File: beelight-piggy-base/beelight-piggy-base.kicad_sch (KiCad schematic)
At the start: 85 parts, among them J1 B_Le, J10 USB C power only, J2 B_Ri, J4 WS2812_ext, J5 Conn_01x07_Pin, J6 BatSide, J7 DevSide, J8 B_Ri, J9 B_Le, Q1 AO3400A, SW1 SW_Push, U2 BMA253, U3 TPS22917LDBV, U4 rysta, U5 VEML3328, U6 TSOP382xx, U7 MP2667, U8 BQ27421-G1

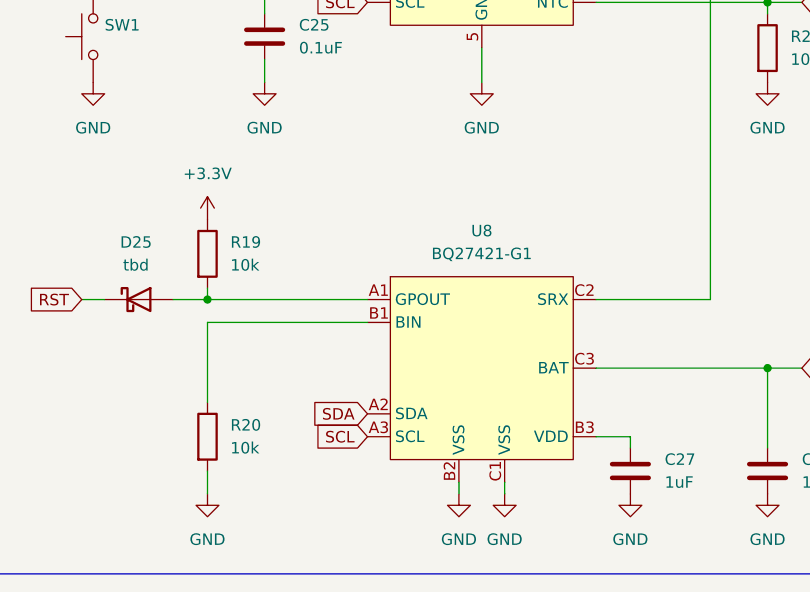
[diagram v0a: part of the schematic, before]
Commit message: rewire gpout pull-up to vdd
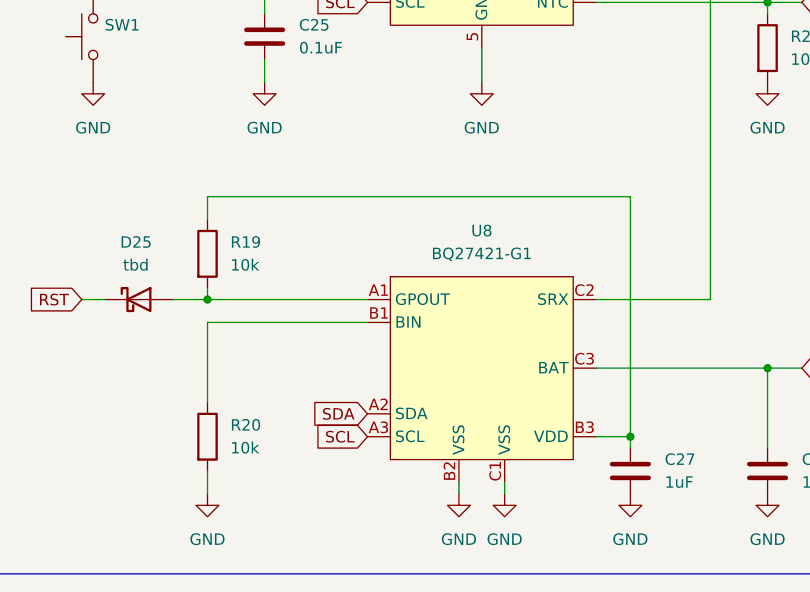
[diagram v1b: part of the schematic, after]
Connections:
- net +3.3V: no longer R19.1
- net at C27.1, U8.B3 (VDD): now also R19.1
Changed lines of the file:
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@@
 	)
 	(junction
+		(at 165.1 241.3)
+		(diameter 0)
+		(color 0 0 0 0)
+	)
+	(junction
 		(at 370.84 120.65)
 		(diameter 0)
@@
 	(wire
 		(pts
+			(xy 165.1 214.63) (xy 165.1 241.3)
+		)
+		(stroke
+			(width 0)
+			(type default)
+		)
+	)
+	(wire
+		(pts
 			(xy 267.97 227.33) (xy 267.97 226.06)
 		)
@@
 	(wire
 		(pts
+			(xy 118.11 217.17) (xy 118.11 214.63)
+		)
+		(stroke
+			(width 0)
+			(type default)
+		)
+	)
+	(wire
+		(pts
 			(xy 261.62 43.18) (xy 261.62 179.07)
 		)
@@
 	(wire
 		(pts
+			(xy 118.11 214.63) (xy 165.1 214.63)
+		)
+		(stroke
+			(width 0)
+			(type default)
+		)
+	)
+	(wire
+		(pts
 			(xy 76.2 120.65) (xy 86.36 120.65)
 		)
@@
 					(unit 1)
 				)
-			)
-		)
-	)
-	(symbol
-		(lib_id "power:+3.3V")
-		(at 118.11 217.17 0)
-		(mirror y)
-		(unit 1)
-		(body_style 1)
-		(exclude_from_sim no)
-		(in_bom yes)
-		(on_board yes)
-		(in_pos_files yes)
-		(dnp no)
-		(property "Reference" "#PWR055"
-			(at 118.11 220.98 0)
-			(hide yes)
-			(show_name no)
-			(do_not_autoplace no)
-			(effects
-				(font
-					(size 1.27 1.27)
-				)
-			)
-		)
-		(property "Value" "+3.3V"
-			(at 118.11 212.09 0)
-			(show_name no)
-			(do_not_autoplace no)
-			(effects
-				(font
-					(size 1.27 1.27)
-				)
-			)
-		)
-		(property "Footprint" ""
-			(at 118.11 217.17 0)
-			(hide yes)
-			(show_name no)
-			(do_not_autoplace no)
-			(effects
-				(font
-					(size 1.27 1.27)
-				)
-			)
-		)
-		(property "Datasheet" ""
-			(at 118.11 217.17 0)
-			(hide yes)
-			(show_name no)
-			(do_not_autoplace no)
-			(effects
-				(font
-					(size 1.27 1.27)
-				)
-			)
-		)
-		(property "Description" "Power symbol creates a global label with name \"+3.3V\""
-			(at 118.11 217.17 0)
-			(hide yes)
-			(show_name no)
-			(do_not_autoplace no)
-			(effects
-				(font
-					(size 1.27 1.27)
-				)
-			)
-		)
-		(pin "1"
-		)
-		(instances
-			(project "beelight-piggy-base"
-				(path "/22ed276f-7cd6-4eef-b98c-6265ea08505b"
-					(reference "#PWR055")
-					(unit 1)
-				)

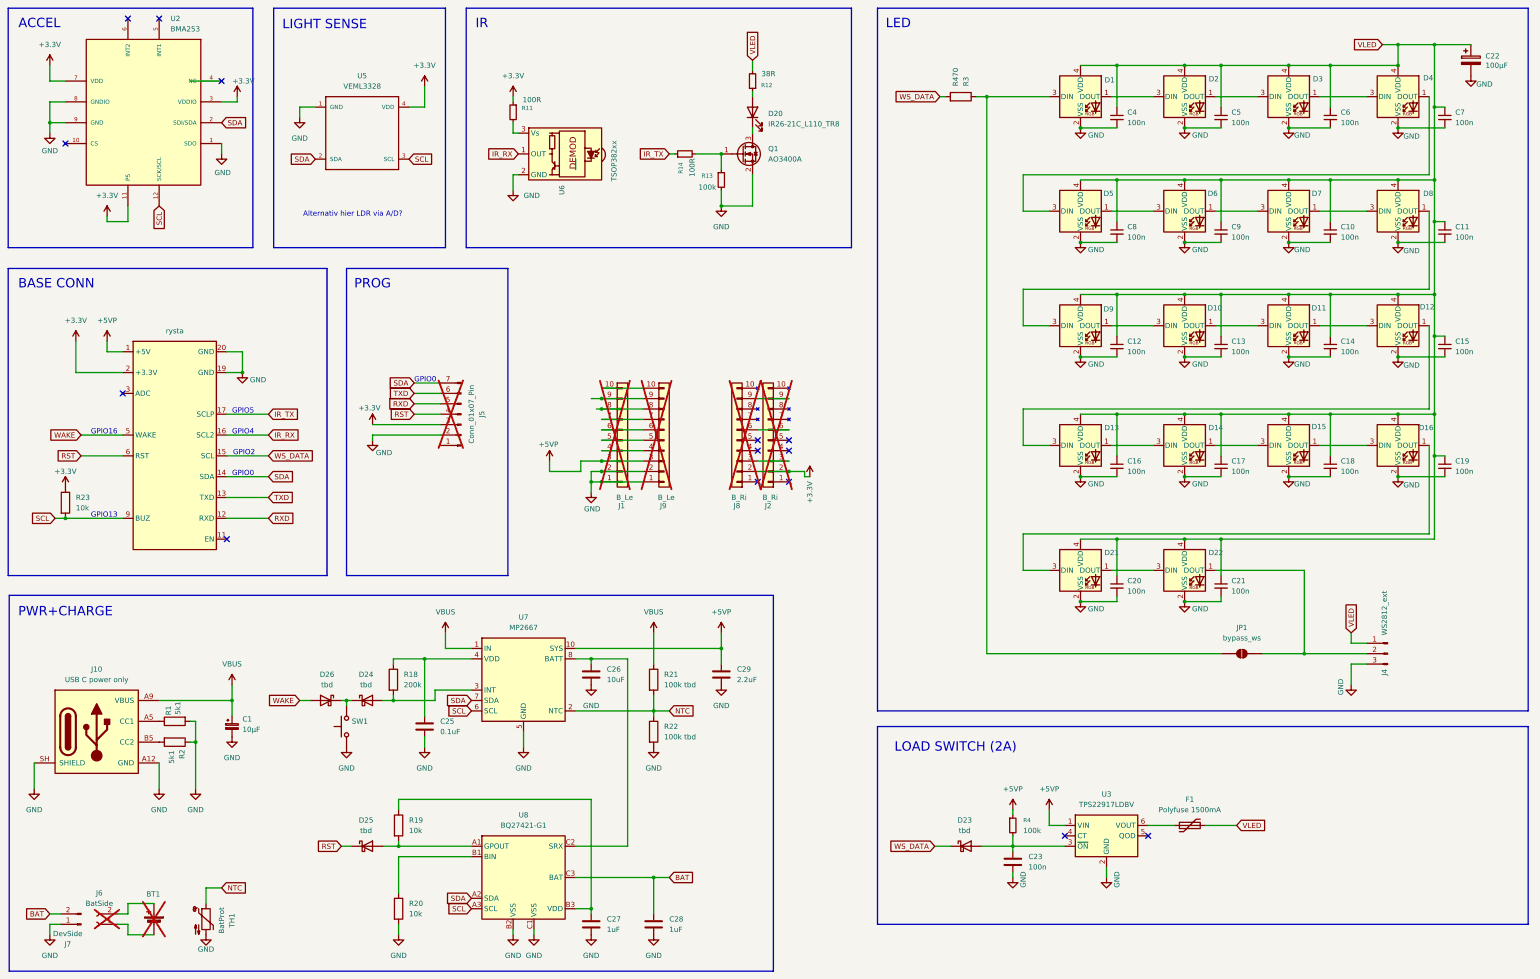
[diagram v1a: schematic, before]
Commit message: ws2816, schottky diodes added, used 0r for jprs
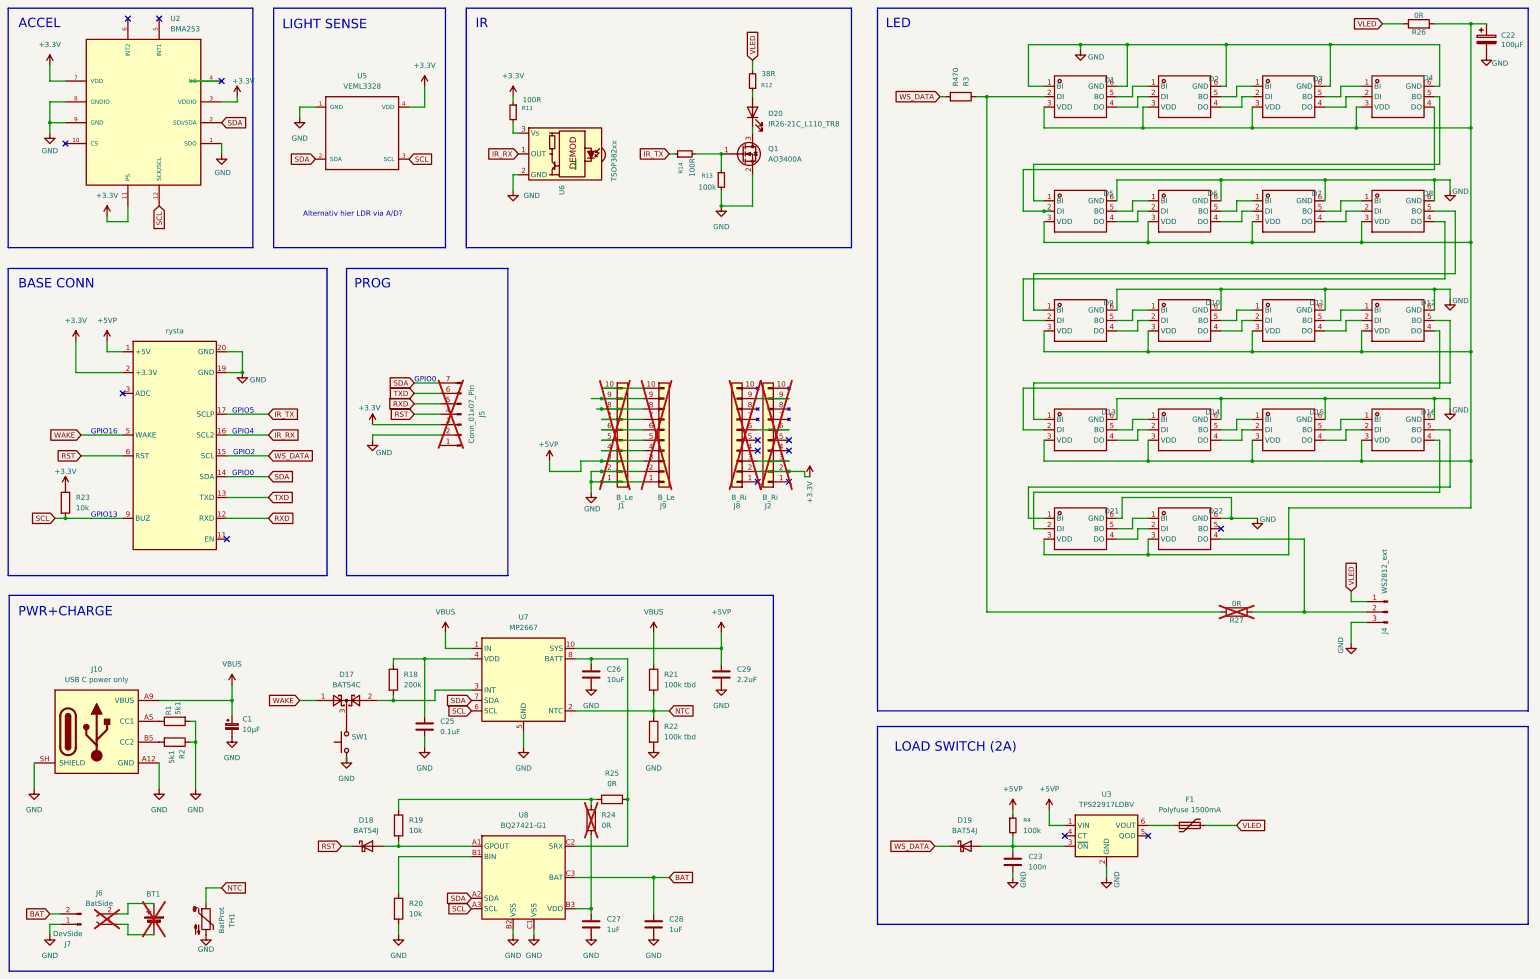
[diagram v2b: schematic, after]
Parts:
- removed C10, C11, C12, C13, C14, C15, C16, C17, C18, C19, C20, C21, C4, C5, C6, C7, C8, C9: 100n, Capacitor_SMD:C_0402_1005Metric, symbol Device:C_Small
- removed D10, D11, D12, D13, D14, D15, D16, D9: WS2812B, LED_SMD:LED_WS2812B-2020_PLCC4_2.0x2.0mm, symbol LED:WS2812B-2020
- removed D23, D24, D25, D26: tbd, symbol .local:D_Schottky
- removed JP1: bypass_ws, Jumper:SolderJumper-2_P1.3mm_Open_RoundedPad1.0x1.5mm, symbol Jumper:SolderJumper_2_Open
- added D10, D11, D12, D13, D14, D15, D16, D9: WS2812B, EasyEDA_Lib:LED-SMD_6P-L2.2-W2.0_WS2816B-2020, symbol EasyEDA_Lib:WS2816B-2020
- added D17: BAT54C, Package_TO_SOT_SMD:SOT-23, symbol Diode:BAT54C
- added D18, D19: BAT54J, Diode_SMD:D_SOD-323F, symbol Diode:BAT54J
- added R24, R25, R26, R27: 0R, Resistor_SMD:R_0402_1005Metric, symbol .local:R
- C23: footprint (none) -> Capacitor_SMD:C_0402_1005Metric
- C25, C27: footprint .local:C_0402_1005Metric -> Capacitor_SMD:C_0402_1005Metric
- C26: footprint .local:C_0805_2012Metric -> Capacitor_SMD:C_0805_2012Metric
- C28, C29: footprint .local:C_0603_1608Metric -> Capacitor_SMD:C_0603_1608Metric
- D1, D2, D21, D22, D3, D4, D5, D6, D7, D8: footprint LED_SMD:LED_WS2812B-2020_PLCC4_2.0x2.0mm -> EasyEDA_Lib:LED-SMD_6P-L2.2-W2.0_WS2816B-2020; symbol LED:WS2812B-2020 -> EasyEDA_Lib:WS2816B-2020; LCSC Part Name (none) -> SMD灯珠; Manufacturer (none) -> worldsemi; Manufacturer Part (none) -> WS2816B-2020; Supplier (none) -> LCSC; Supplier Part (none) -> C4154877
- R1, R11, R12, R13, R14, R2, R3: footprint Resistor_SMD:R_0805_2012Metric -> Resistor_SMD:R_0402_1005Metric
- R18, R19, R20, R21, R22, R23: footprint .local:R_0402_1005Metric -> Resistor_SMD:R_0402_1005Metric
- R4: footprint (none) -> Resistor_SMD:R_0402_1005Metric
- U2: footprint BMA253:LGA-12 -> beelight:LGA-12
- U7: footprint .local:QFN-10_2x2mm_P0.5mm -> beelight:QFN-10_2x2mm_P0.5mm
- U8: footprint .local:BGA-9_1.6x1.6mm_Layout3x3_P0.5mm -> beelight:BGA-9_1.6x1.6mm_Layout3x3_P0.5mm
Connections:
- net GND: now also D1.1 (BI), D1.6 (GND), D2.6 (GND), D21.6 (GND), D22.6 (GND), D3.6 (GND), D4.6 (GND), D5.6 (GND), D6.6 (GND), D7.6 (GND), D8.6 (GND), D10.6 (GND), D11.6 (GND), D12.6 (GND), D13.6 (GND), D14.6 (GND), D15.6 (GND), D16.6 (GND), D9.6 (GND); no longer D1.2 (VSS), D2.2 (VSS), D21.2 (VSS), D22.2 (VSS), D3.2 (VSS), D4.2 (VSS), D5.2 (VSS), D6.2 (VSS), D7.2 (VSS), D8.2 (VSS)
- net RST: now also D18.1 (K)
- net VLED: now also R26.1; no longer C22.1, D1.4 (VDD), D2.4 (VDD), D21.4 (VDD), D22.4 (VDD), D3.4 (VDD), D4.4 (VDD), D5.4 (VDD), D6.4 (VDD), D7.4 (VDD), D8.4 (VDD)
- net WAKE: now also D17.1
- net WS_DATA: now also D19.1 (K)
- net at R18.2, U7.3 (INT): now also D17.2
- net at C26.1, U7.8 (BATT), U7.9 (BATT)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: now also R25.2
- net at C23.1, R4.2, U3.3 (~{ON}): now also D19.2 (A)
- net at J4.2 (Pin_2): now also D22.4 (DO), R27.2; no longer D22.1 (DOUT)
- net at D1.3 (VDD): now also C22.1, D2.3 (VDD), D21.3 (VDD), D22.3 (VDD), D3.3 (VDD), D4.3 (VDD), D5.3 (VDD), D6.3 (VDD), D7.3 (VDD), D8.3 (VDD), D10.3 (VDD), D11.3 (VDD), D12.3 (VDD), D13.3 (VDD), D14.3 (VDD), D15.3 (VDD), D16.3 (VDD), D9.3 (VDD), R26.2; no longer R3.1
- net at D5.1 (BI): now also D4.5 (BO); no longer D6.3 (DIN)
- net at D4.1 (BI): now also D3.5 (BO); no longer D5.3 (DIN)
- net at SW1.2: now also D17.3
- net at D8.1 (BI): now also D7.5 (BO)
- net at D7.1 (BI): now also D6.5 (BO); no longer D8.3 (DIN)
- net at D2.1 (BI): now also D1.5 (BO); no longer D3.3 (DIN)
- net at R19.2, U8.A1 (GPOUT): now also D18.2 (A)
- net at C27.1, U8.B3 (VDD): now also R24.1; no longer R19.1
- net at D3.1 (BI): now also D2.5 (BO); no longer D4.3 (DIN)
- net at D21.1 (BI): now also D16.5 (BO); no longer D22.3 (DIN)
- net at D6.1 (BI): now also D5.5 (BO); no longer D7.3 (DIN)
- new net: D15.5 (BO), D16.1 (BI)
- new net: D15.4 (DO), D16.2 (DI)
- new net: D16.4 (DO), D21.2 (DI)
- new net: D14.5 (BO), D15.1 (BI)
- new net: D14.4 (DO), D15.2 (DI)
- new net: D4.4 (DO), D5.2 (DI)
- new net: D5.4 (DO), D6.2 (DI)
- new net: D12.5 (BO), D13.1 (BI)
- new net: D12.4 (DO), D13.2 (DI)
- new net: D13.4 (DO), D14.2 (DI)
- new net: D13.5 (BO), D14.1 (BI)
- new net: D7.4 (DO), D8.2 (DI)
- new net: D8.4 (DO), D9.2 (DI)
- new net: D8.5 (BO), D9.1 (BI)
- new net: D1.4 (DO), D2.2 (DI)
- new net: D2.4 (DO), D3.2 (DI)
- new net: D10.2 (DI), D9.4 (DO)
- new net: D10.1 (BI), D9.5 (BO)
- new net: D10.4 (DO), D11.2 (DI)
- new net: D10.5 (BO), D11.1 (BI)
- new net: D11.5 (BO), D12.1 (BI)
- new net: D11.4 (DO), D12.2 (DI)
- new net: D3.4 (DO), D4.2 (DI)
- new net: D21.4 (DO), D22.2 (DI)
- new net: D21.5 (BO), D22.1 (BI)
- new net: D1.2 (DI), R27.1, R3.1
- new net: D6.4 (DO), D7.2 (DI)
- new net: R19.1, R24.2, R25.1
- no-connect marks 14 -> 15
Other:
- moved on the sheet: C22, J4, SW1

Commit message: pre jlc proto order
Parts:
- added J11: ExtWSSolderPads, Crystal:Resonator_SMD-3Pin_7.2x3.0mm_HandSoldering, symbol Connector_Generic:Conn_01x03
- added J3: BatSolderPads, Diode_SMD:D_2114_3652Metric_Pad1.85x3.75mm_HandSolder, symbol Connector_Generic:Conn_01x02
- C1: value 10µF -> 10uF
- C23: value 100n -> 100nF
- C25: value 0.1uF -> 100nF
- F1: footprint Fuse:Fuse_1812_4532Metric -> EasyEDA_Lib:F0805; symbol Device:Polyfuse -> EasyEDA_Lib:BSMD0805-050-12V; LCSC Part Name (none) -> 12V 0.5A 0805自恢复; Manufacturer (none) -> BHFUSE(佰宏); Manufacturer Part (none) -> BSMD0805-050-12V; Supplier (none) -> LCSC; Supplier Part (none) -> C2977522
- J1, J2, J8, J9, R24, R27: now left out of the parts list
- J10: footprint .local:USB_C_Receptacle_GCT_USB4125-xx-x_6P_TopMnt_Horizontal -> Connector_USB:USB_C_Receptacle_GCT_USB4125-xx-x_6P_TopMnt_Horizontal
- J4, J7, U4: now not fitted; now left out of the parts list
- R21: value 100k tbd -> 6.34k
- R22: value 100k tbd -> 22.1k
- SW1: footprint (none) -> Button_Switch_SMD:SW_Push_SPST_NO_Alps_SKRK; now not fitted; now left out of the parts list
- U6: now not fitted
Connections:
- net BAT: now also J3.1 (Pin_1)
- net GND: now also J11.3 (Pin_3), J3.2 (Pin_2)
- net VLED: now also F1.1, J11.1 (Pin_1); no longer F1.2
- net at C26.1, U7.8 (BATT), U7.9 (BATT)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: now also R25.1; no longer R25.2
- net at D22.4 (DO), J4.2 (Pin_2), R27.2: now also J11.2 (Pin_2)
- net at U3.6 (VOUT): now also F1.2; no longer F1.1
- net at R19.1, R24.2: now also R25.2; no longer R25.1
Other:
- moved on the sheet: R25

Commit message: last minor fixes pre order
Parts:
- added C30, C31, C32: 100nF, Capacitor_SMD:C_0402_1005Metric, symbol .local:C
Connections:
- net +3.3V: now also C30.1, C31.1, C32.1
- net GND: now also C30.2, C31.2, C32.2

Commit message: PROTOTYPE ORDER - minor fixes + new board outline
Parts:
- R24, R25, R26, R27: footprint Resistor_SMD:R_0402_1005Metric -> Resistor_SMD:R_1206_3216Metric
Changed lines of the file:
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@@
 			)
 		)
-		(property "Footprint" "Resistor_SMD:R_0402_1005Metric"
+		(property "Footprint" "Resistor_SMD:R_1206_3216Metric"
 			(at 367.03 27.178 90)
 			(hide yes)
@@
 			)
 		)
-		(property "Footprint" "Resistor_SMD:R_0402_1005Metric"
+		(property "Footprint" "Resistor_SMD:R_1206_3216Metric"
 			(at 322.58 170.688 90)
 			(hide yes)
@@
 			)
 		)
-		(property "Footprint" "Resistor_SMD:R_0402_1005Metric"
+		(property "Footprint" "Resistor_SMD:R_1206_3216Metric"
 			(at 170.18 216.408 90)
 			(hide yes)
@@
 			)
 		)
-		(property "Footprint" "Resistor_SMD:R_0402_1005Metric"
+		(property "Footprint" "Resistor_SMD:R_1206_3216Metric"
 			(at 166.878 219.71 90)
 			(hide yes)
